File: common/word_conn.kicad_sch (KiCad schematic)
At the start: 1 part, among them J4 Conn_02x08_Top_Bottom

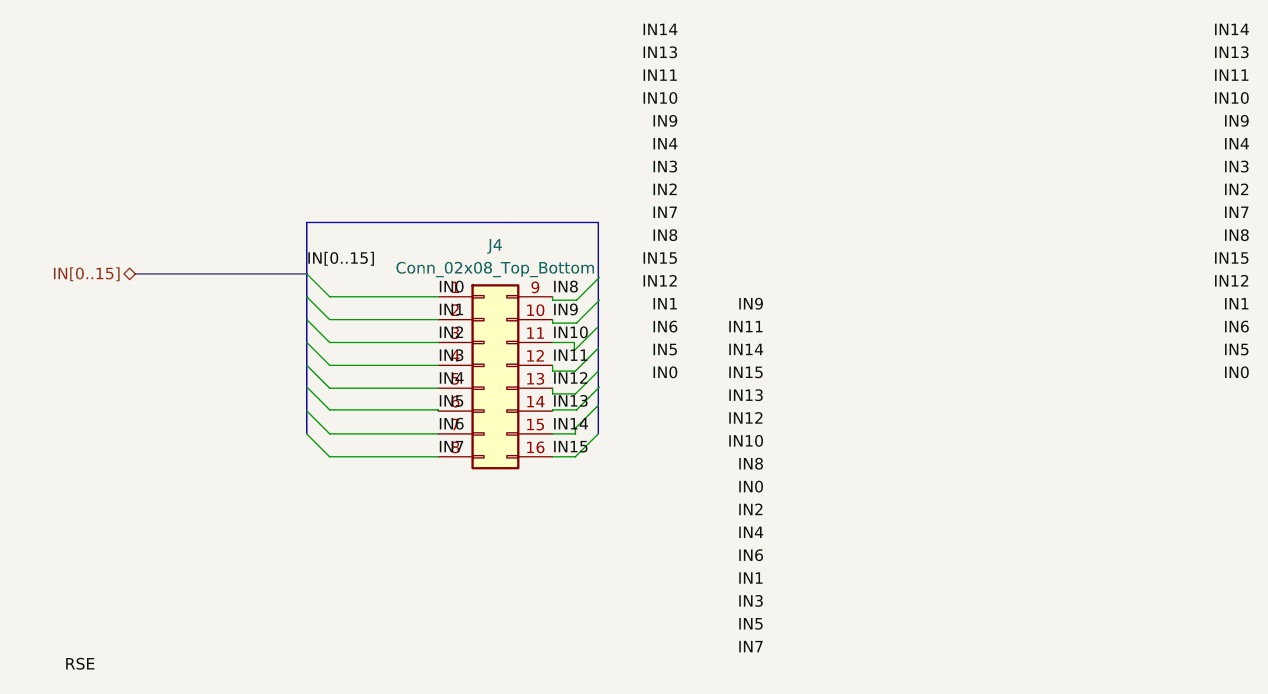
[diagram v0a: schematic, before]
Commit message: Memory Controller fabrication checks complete
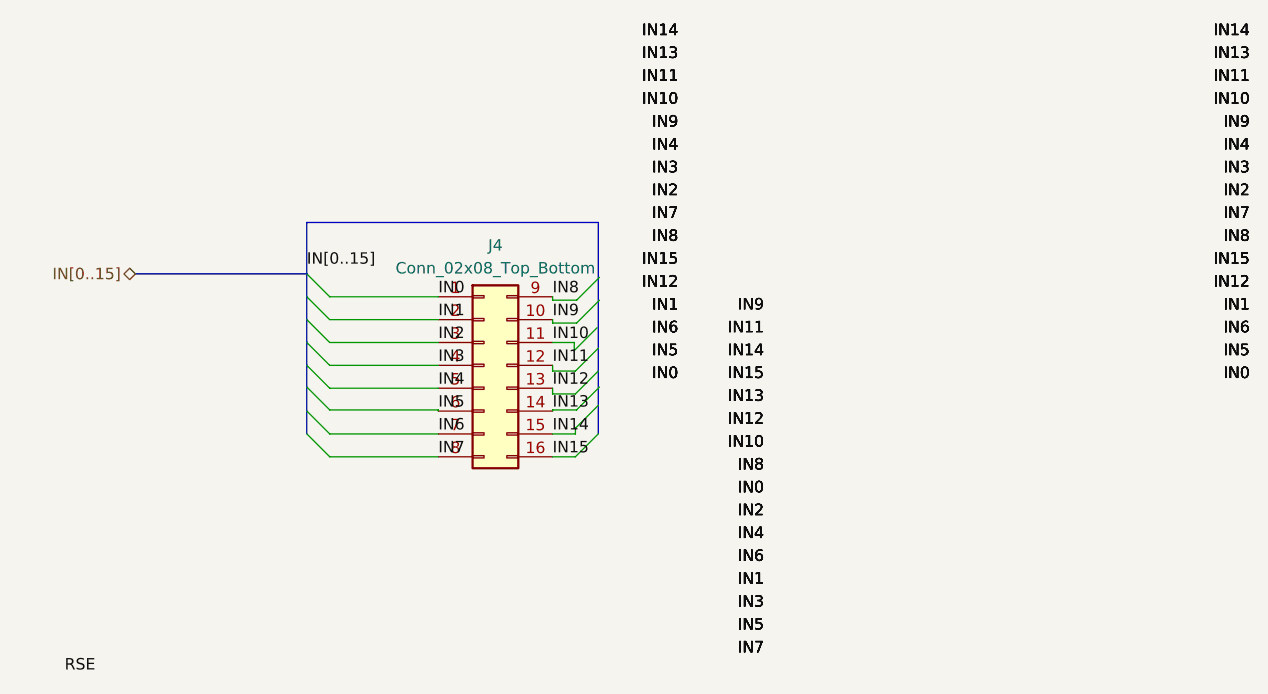
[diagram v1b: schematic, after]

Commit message: Cleanup, added photos and README overhaul
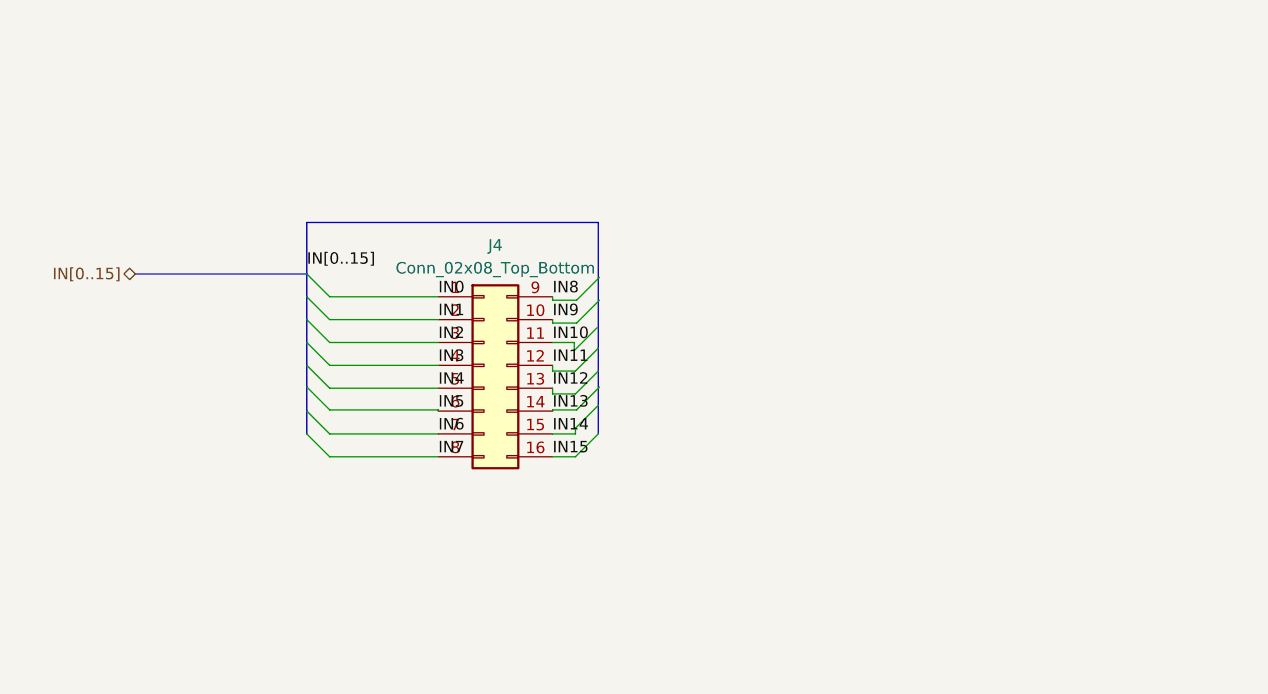
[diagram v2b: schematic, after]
